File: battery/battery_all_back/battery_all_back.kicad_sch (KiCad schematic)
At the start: 20 parts

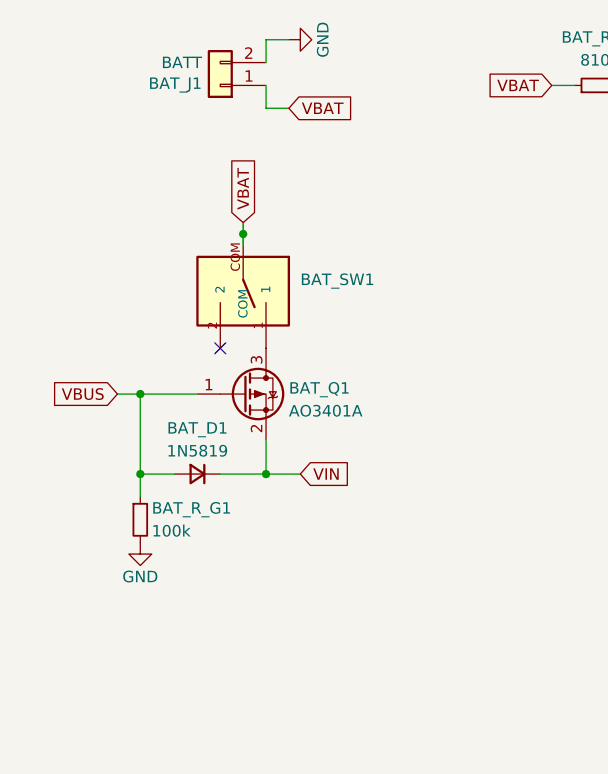
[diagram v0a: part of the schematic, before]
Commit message: update battery switch symbol
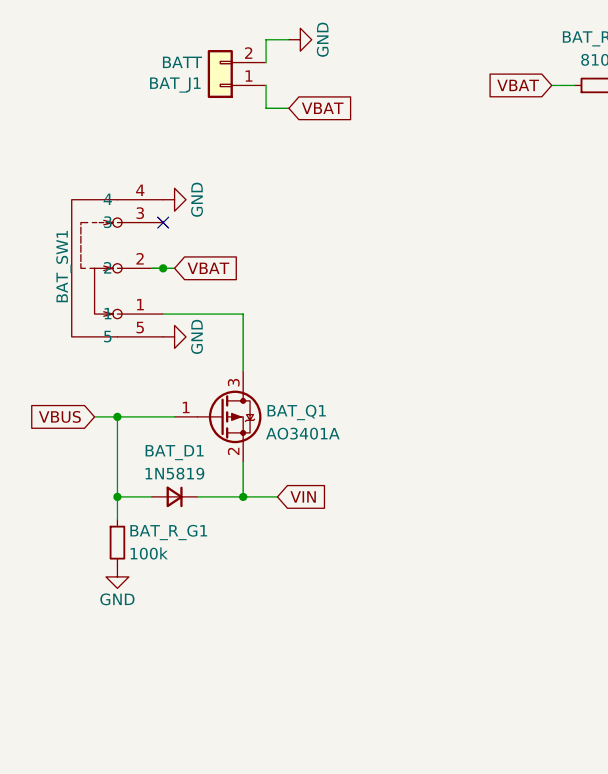
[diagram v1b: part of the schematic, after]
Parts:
- BAT_Q1: footprint ErgoCai.pretty:SOT-23 -> Package_TO_SOT_SMD:SOT-23
- BAT_SW1: footprint ErgoCai.pretty:SK12D07VG4 -> easyeda2kicad:SW-TH_SK12D07VG4; LCSC Part (none) -> C393937
- BAT_TP1: footprint ErgoCai.pretty:SOIC-8-1EP_3.9x4.9mm_P1.27mm_EP2.29x3mm -> Package_SO:SOIC-8-1EP_3.9x4.9mm_P1.27mm_EP2.29x3mm
- BAT_U1: footprint ErgoCai.pretty:SOT-23-5_L3.0-W1.7-P0.95-LS2.8-BR -> easyeda2kicad:SOT-23-5_L3.0-W1.7-P0.95-LS2.8-BR
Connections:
- net GND: now also BAT_SW1.4, BAT_SW1.5
- net VBAT: now also BAT_SW1.2; no longer BAT_SW1.COM
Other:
- moved on the sheet: BAT_D1, BAT_Q1, BAT_R_G1

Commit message: remove default battery
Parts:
- BAT_C1, BAT_C2, BAT_C3: footprint Capacitor_SMD:C_0603_1608Metric -> ErgoCai.pretty:C_0603_1608Metric
- BAT_L1: footprint Inductor_SMD:L_0603_1608Metric -> ErgoCai.pretty:L_0603_1608Metric
- BAT_Q1: footprint Package_TO_SOT_SMD:SOT-23 -> ErgoCai.pretty:SOT-23
- BAT_SW1: footprint easyeda2kicad:SW-TH_SK12D07VG4 -> ErgoCai.pretty:SW-TH_SK12D07VG4
- BAT_TP1: footprint Package_SO:SOIC-8-1EP_3.9x4.9mm_P1.27mm_EP2.29x3mm -> ErgoCai.pretty:SOIC-8-1EP_3.9x4.9mm_P1.27mm_EP2.29x3mm
- BAT_U1: footprint easyeda2kicad:SOT-23-5_L3.0-W1.7-P0.95-LS2.8-BR -> ErgoCai.pretty:SOT-23-5_L3.0-W1.7-P0.95-LS2.8-BR
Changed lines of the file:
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@@
 			)
 		)
-		(property "Footprint" "easyeda2kicad:SOT-23-5_L3.0-W1.7-P0.95-LS2.8-BR"
+		(property "Footprint" "ErgoCai.pretty:SOT-23-5_L3.0-W1.7-P0.95-LS2.8-BR"
 			(at 132.08 121.92 0)
 			(effects
@@
 			)
 		)
-		(property "Footprint" "easyeda2kicad:SW-TH_SK12D07VG4"
+		(property "Footprint" "ErgoCai.pretty:SW-TH_SK12D07VG4"
 			(at 71.12 66.04 0)
 			(effects
@@
 			)
 		)
-		(property "Footprint" "Capacitor_SMD:C_0603_1608Metric"
+		(property "Footprint" "ErgoCai.pretty:C_0603_1608Metric"
 			(at 107.6452 137.16 0)
 			(effects
@@
 			)
 		)
-		(property "Footprint" "Inductor_SMD:L_0603_1608Metric"
+		(property "Footprint" "ErgoCai.pretty:L_0603_1608Metric"
 			(at 146.05 129.54 0)
 			(effects
@@
 			)
 		)
-		(property "Footprint" "Package_TO_SOT_SMD:SOT-23"
+		(property "Footprint" "ErgoCai.pretty:SOT-23"
 			(at 87.63 84.455 0)
 			(effects
@@
 			)
 		)
-		(property "Footprint" "Capacitor_SMD:C_0603_1608Metric"
+		(property "Footprint" "ErgoCai.pretty:C_0603_1608Metric"
 			(at 167.3352 137.16 0)
 			(effects
@@
 			)
 		)
-		(property "Footprint" "Capacitor_SMD:C_0603_1608Metric"
+		(property "Footprint" "ErgoCai.pretty:C_0603_1608Metric"
 			(at 180.0352 137.16 0)
 			(effects
@@
 			)
 		)
-		(property "Footprint" "Package_SO:SOIC-8-1EP_3.9x4.9mm_P1.27mm_EP2.29x3mm"
+		(property "Footprint" "ErgoCai.pretty:SOIC-8-1EP_3.9x4.9mm_P1.27mm_EP2.29x3mm"
 			(at 179.07 86.36 0)
 			(effects

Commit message: add power switch
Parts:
- removed BAT_SW1: ~, ErgoCai.pretty:SW-TH_SK12D07VG4, symbol ErgoCai:SK12D07VG4
- renumbered BAT_R_PRG1 to BAT_R_P1
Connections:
- net VSYS: now reaches BAT_Q1.3 (D)
- no-connect marks 1 -> 0

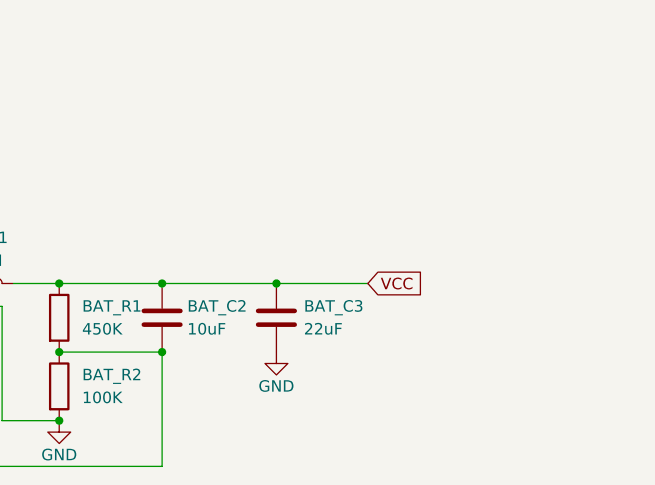
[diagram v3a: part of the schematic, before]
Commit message: update to 3.3V tag
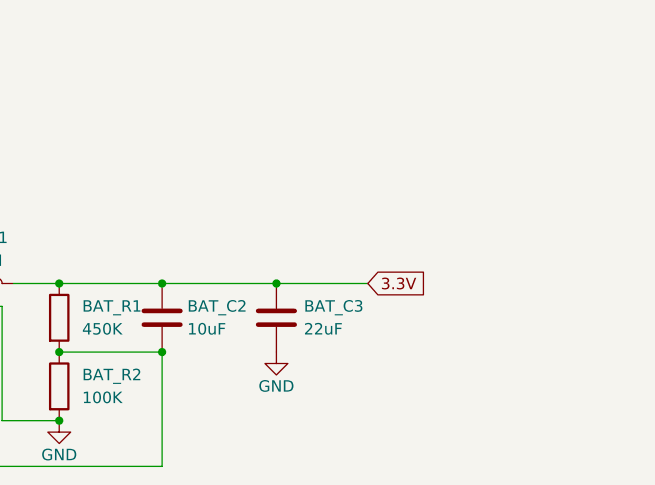
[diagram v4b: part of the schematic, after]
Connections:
- net VCC renamed 3.3V
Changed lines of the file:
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@@
 		)
 	)
-	(global_label "VCC"
+	(global_label "3.3V"
 		(shape input)
 		(at 189.23 129.54 0)
@@
 		)
 		(property "Intersheetrefs" "${INTERSHEET_REFS}"
-			(at 195.8438 129.54 0)
+			(at 196.3276 129.54 0)
 			(effects
 				(font
